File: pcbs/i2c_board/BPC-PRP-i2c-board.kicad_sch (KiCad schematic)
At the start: 16 parts, among them J1 Power, J2 I2C, J3 I2C_Aux, J4 ADC, J5 I2C_Aux

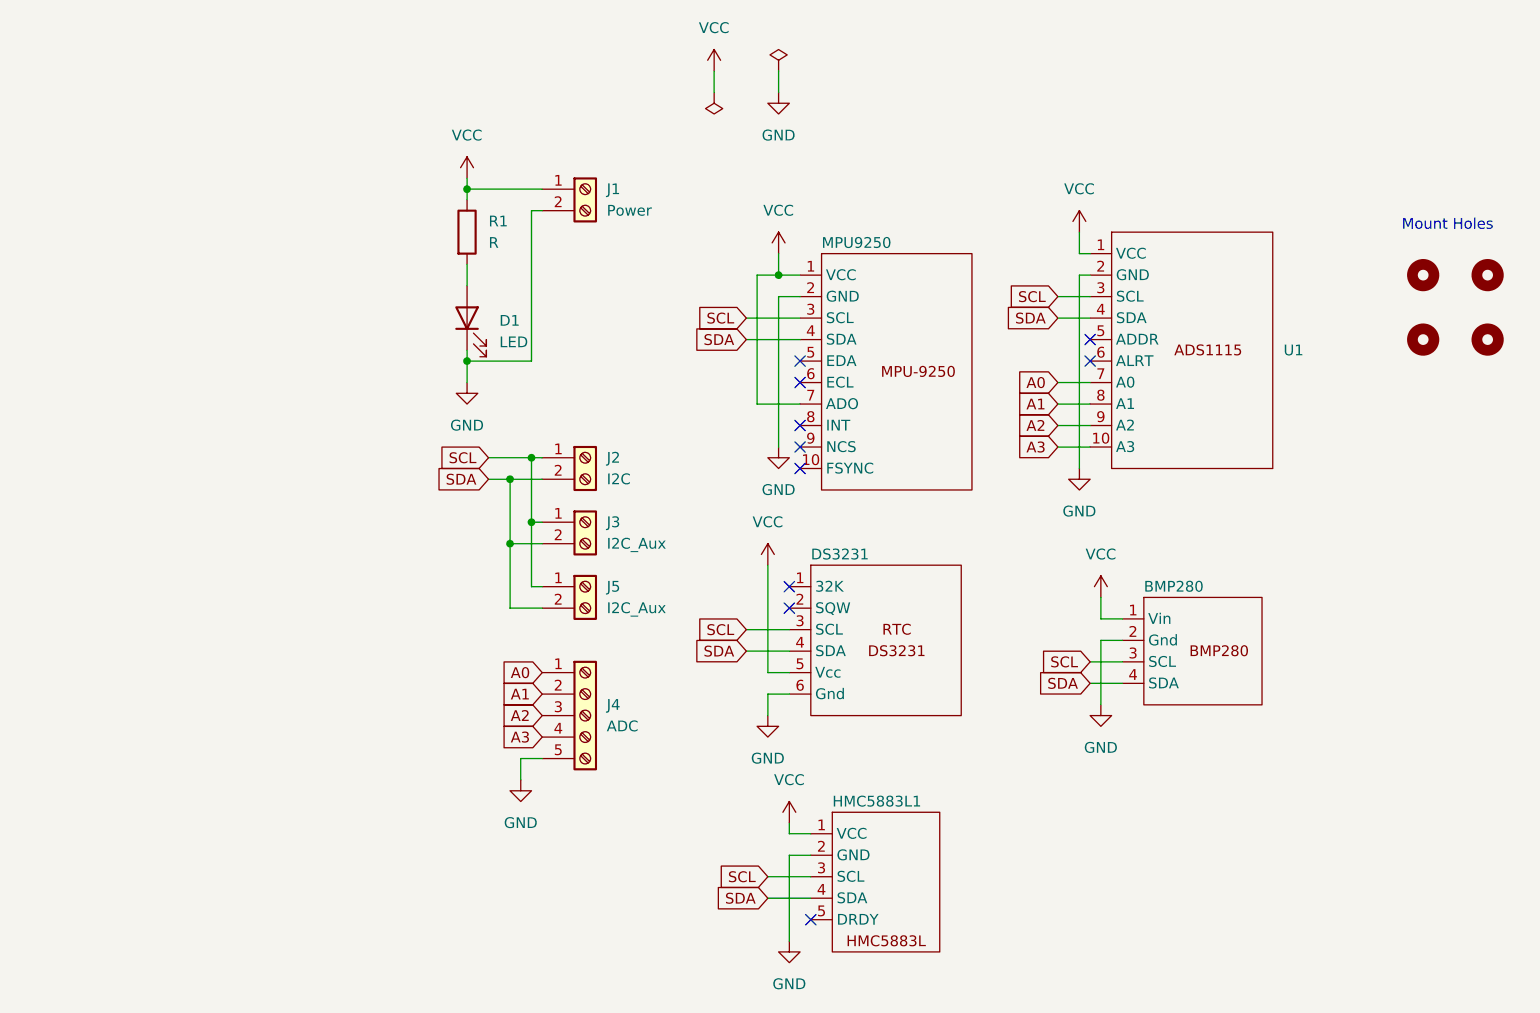
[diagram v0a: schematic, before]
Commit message: add i2c pullups for rpi ext and i2c board
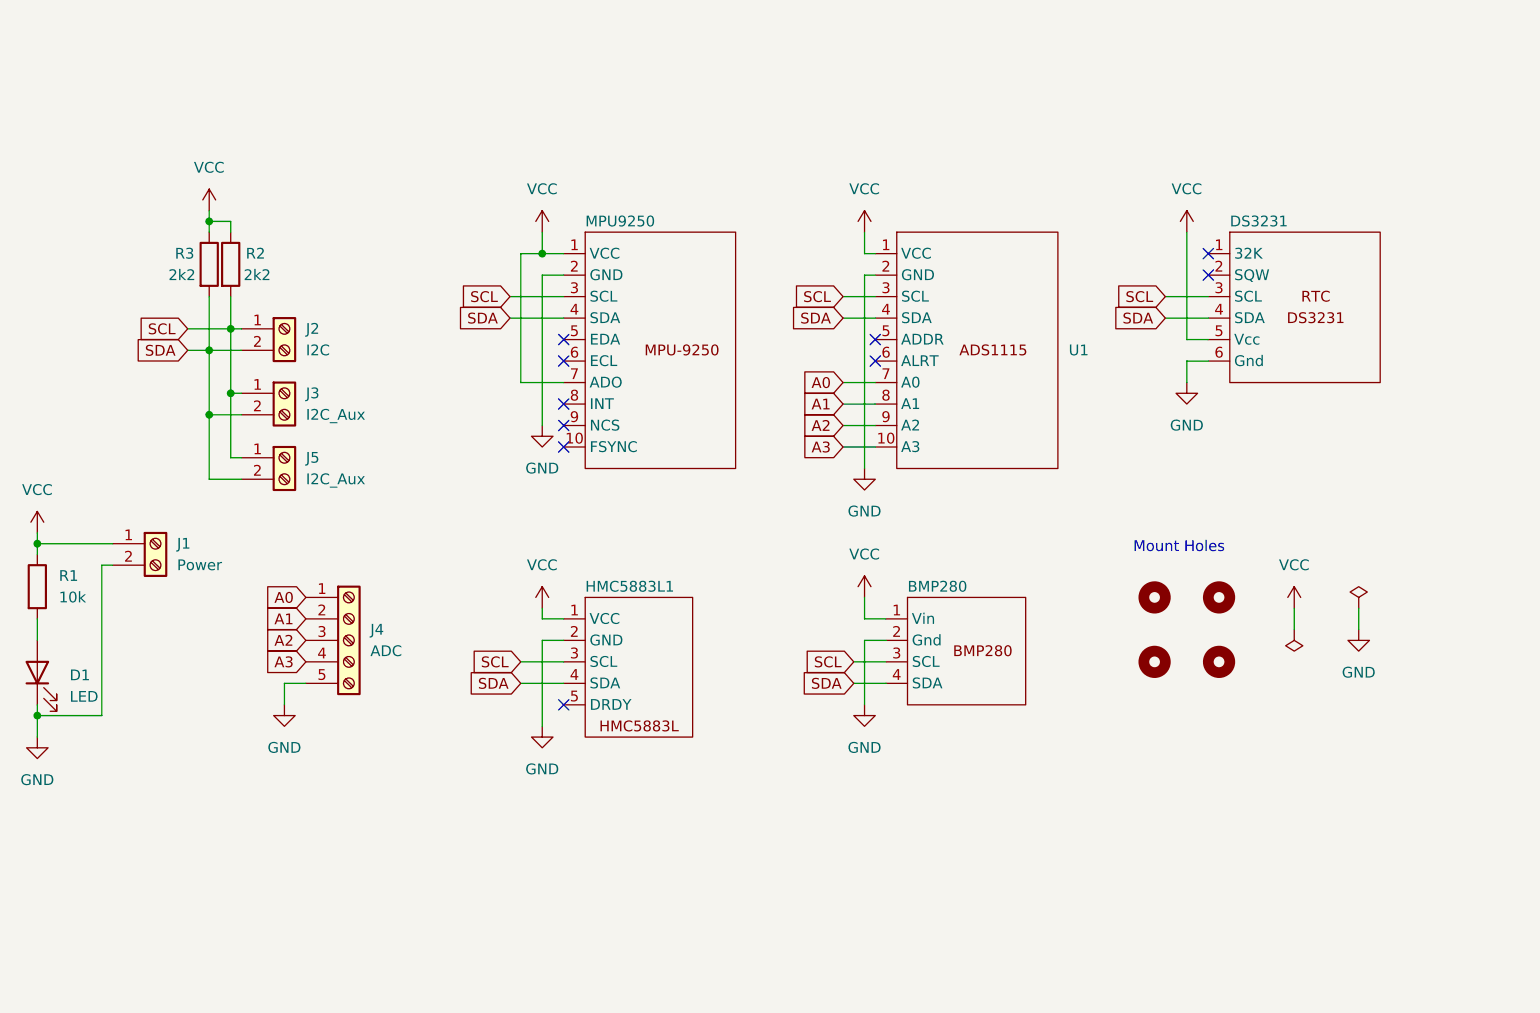
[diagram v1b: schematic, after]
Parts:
- added R2, R3: 2k2, Resistor_SMD:R_1206_3216Metric, symbol Device:R
- R1: value R -> 10k
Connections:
- net SCL: now also R2.2
- net SDA: now also R3.2
- net VCC: now also R2.1, R3.1
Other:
- moved on the sheet: BMP280, D1, DS3231, HMC5883L1, J1, J2, J3, J4, J5, MPU9250, R1, U1
